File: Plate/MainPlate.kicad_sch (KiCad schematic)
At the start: 3 parts, among them J1 Conn_01x03, SW1 Test, SW2 Service

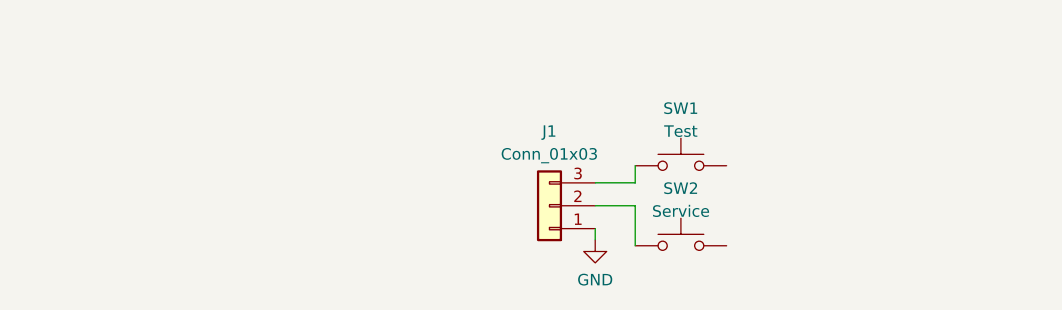
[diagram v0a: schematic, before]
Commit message: Move buttons, add totally 100% real LEDs to plate
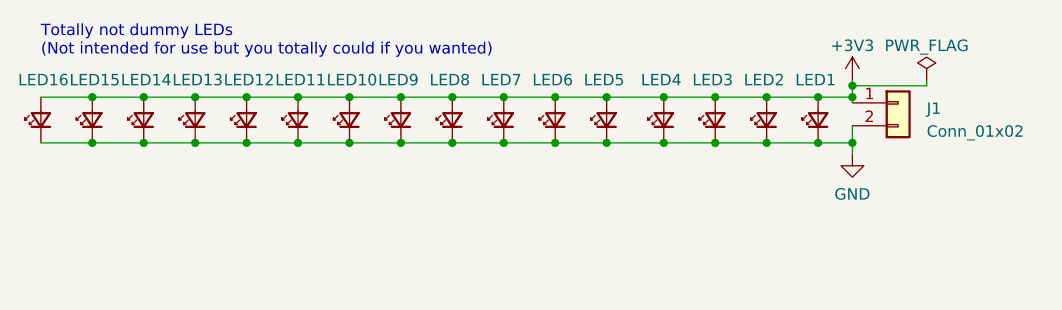
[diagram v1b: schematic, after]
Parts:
- removed J1: Conn_01x03, Connector_PinHeader_2.54mm:PinHeader_1x03_P2.54mm_Vertical, symbol Connector_Generic:Conn_01x03
- removed SW1: Test, Button_Switch_THT:SW_Tactile_SPST_Angled_PTS645Vx39-2LFS, symbol Switch:SW_Push
- removed SW2: Service, Button_Switch_THT:SW_Tactile_SPST_Angled_PTS645Vx39-2LFS, symbol Switch:SW_Push
- added J1: Conn_01x02, Connector_PinHeader_2.54mm:PinHeader_1x02_P2.54mm_Vertical, symbol Connector_Generic:Conn_01x02
- added LED1, LED10, LED11, LED12, LED13, LED14, LED15, LED16, LED2, LED3, LED4, LED5, LED6, LED7, LED8, LED9: LED_Small, LED_SMD:LED_0805_2012Metric_Pad1.15x1.40mm_HandSolder, symbol Device:LED_Small
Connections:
- net GND: now also J1.2 (Pin_2), LED1.1 (K), LED10.1 (K), LED11.1 (K), LED12.1 (K), LED13.1 (K), LED14.1 (K), LED15.1 (K), LED16.1 (K), LED2.1 (K), LED3.1 (K), LED4.1 (K), LED5.1 (K), LED6.1 (K), LED7.1 (K), LED8.1 (K), LED9.1 (K)
- new net +3V3: J1.1 (Pin_1), LED1.2 (A), LED10.2 (A), LED11.2 (A), LED12.2 (A), LED13.2 (A), LED14.2 (A), LED15.2 (A), LED16.2 (A), LED2.2 (A), LED3.2 (A), LED4.2 (A), LED5.2 (A), LED6.2 (A), LED7.2 (A), LED8.2 (A), LED9.2 (A)
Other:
- note added: "Totally not dummy LEDs (Not intended for use but you totally could if you wanted)"
